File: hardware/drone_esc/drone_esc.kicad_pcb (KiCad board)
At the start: 2 copper layers, 166 parts, among them Q1 BSC016N04LS, Q10 BSC016N04LS, Q11 BSC016N04LS, Q12 BSC016N04LS, Q13 BSC016N04LS, Q14 BSC016N04LS, Q15 BSC016N04LS, Q16 BSC016N04LS, Q17 BSC016N04LS, Q18 BSC016N04LS, Q19 BSC016N04LS, Q2 BSC016N04LS, Q20 BSC016N04LS, Q21 BSC016N04LS, Q22 BSC016N04LS, Q23 BSC016N04LS, Q24 BSC016N04LS, Q3 BSC016N04LS, Q4 BSC016N04LS, Q5 BSC016N04LS, Q6 BSC016N04LS, Q7 BSC016N04LS, Q8 BSC016N04LS, Q9 BSC016N04LS, U1 AMS1117-3.3, U10 FD6288Q, U2 INA180A3, U3 STM32G071GBUxN, U4 FD6288Q, U5 STM32G071GBU6, U6 FD6288Q, U7 FD6288Q, U8 STM32G071GBU6, U9 STM32G071GBU6

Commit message: continued developing the pcb board
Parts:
- C12, C14, C16, C21, C22, C23, C31, C32, C33, C47, C48, C49: value 47uF 35V X7R MLCC -> 22uF 25V X5R MLCC; footprint Capacitor_SMD:C_2220_5750Metric -> Capacitor_SMD:C_1210_3225Metric; moved to B.Cu
- moved C12 92.1 mm to (-8.50, -9.00), turned to 90 degrees
- moved C14 90.4 mm to (-8.50, 9.00), turned to 90 degrees
- moved C33 86.7 mm to (-4.00, -13.0), turned to 180 degrees
- moved C16 78.3 mm to (4.00, 13.0), turned to 180 degrees
- moved C31 73.0 mm to (8.50, -9.00), turned to 90 degrees
- moved C32 72.9 mm to (8.50, -3.00), turned to 90 degrees
- moved C48 53.8 mm to (-8.50, 3.00), turned to 90 degrees
- moved C47 53.4 mm to (-8.50, -3.00), turned to 90 degrees
- moved C49 48.4 mm to (-4.00, 13.0), turned to 180 degrees
- moved C21 35.2 mm to (4.00, -13.0), turned to 180 degrees
- moved C22 32.5 mm to (8.50, 3.00), turned to 90 degrees
- moved C23 32.3 mm to (8.50, 9.00), turned to 90 degrees

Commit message: continued developing the pcb board
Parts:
- C1, C2: value 22uF 25V X7R MLCC -> 22uF 25V X5R MLCC; moved to B.Cu
- Q11, Q9, U1, U2: moved to B.Cu
- moved U2 107.1 mm to (0.00, -17.0), turned to 90 degrees
- moved U1 89.4 mm to (-0.07, 19.5), turned to 90 degrees
- moved Q11 87.0 mm to (-18.7, 3.00), turned to 90 degrees
- moved C2 84.0 mm to (-0.07, 13.0), turned to 180 degrees
- moved C1 80.5 mm to (-0.07, 26.0)
- moved Q9 76.4 mm to (-18.7, 9.00), turned to 90 degrees
- moved Q7 74.1 mm to (-19.3, 26.4), turned to 90 degrees
- moved U10 9.57 mm to (53.5, 25.0)
- moved C16 1.50 mm to (5.50, 13.0)
- moved C49 1.50 mm to (-5.50, 13.0), turned to 0 degrees

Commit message: finnished component placement
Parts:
- added TP11: V, Drone_components:Rectangle test point, F.Cu at (-4.10, -23.1)
- C10, C27, C29, C30, C37, C39, C40, C53, C55, C56, C8, C9: value 0.47uF 25V X7R MLCC -> 1uF 25V X5R MLCC; footprint Capacitor_SMD:C_0603_1608Metric -> Capacitor_SMD:C_0402_1005Metric
- C11, C28, C38, C54: value 4.7uF 25V X7R MLCC -> 10uF 25V X5R MLCC; footprint Capacitor_SMD:C_1206_3216Metric -> Capacitor_SMD:C_0603_1608Metric
- C18, C41, C44, C5: value 4.7uF 10V X7R MLCC -> 4.7uF 10V X5R MLCC; footprint Capacitor_SMD:C_0603_1608Metric -> Capacitor_SMD:C_0402_1005Metric
- C19, C42, C45, C7: footprint Capacitor_SMD:C_01005_0402Metric -> Capacitor_SMD:C_0402_1005Metric
- C3, C4, Q1, Q13, Q15, Q17, Q19, Q21, Q23, Q3, Q5, Q7, R1: moved to B.Cu
- D1, D10, D11, D12, D2, D3, D4, D5, D6, D7, D8, D9: value BAT165 -> RB520S30; footprint Drone_components:BAT165 -> Drone_components:RB520S30
- R15: value YLR25-4-0.25F-W -> ~
- moved TP1 129.2 mm to (-9.11, -4.57)
- moved C7 125.5 mm to (-3.80, -1.18), turned to 90 degrees
- moved C6 125.4 mm to (-5.40, -1.68)
- moved U3 121.5 mm to (-5.14, -4.88), turned to 90 degrees
- moved C5 120.7 mm to (-5.40, -0.65)
- moved C10 118.5 mm to (-11.5, -12.8)
- moved Q3 117.4 mm to (-20.1, -9.00), turned to 90 degrees
- moved C9 117.1 mm to (-11.5, -10.4)
- moved C8 116.0 mm to (-11.5, -8.01)
- moved Q5 113.9 mm to (-8.10, -17.5), turned to 90 degrees
- moved D3 113.8 mm to (-11.2, -11.6), turned to 180 degrees
- moved C42 112.9 mm to (3.78, -14.3), turned to -90 degrees
- moved D2 112.3 mm to (-11.2, -9.21), turned to 180 degrees
- moved R1 111.7 mm to (-2.08, -20.6), turned to 90 degrees
- moved C45 111.4 mm to (3.73, 1.16), turned to -90 degrees
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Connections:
- R15 pad 1: Net-(U2-+) -> VCC
- U2 pad 3: Net-(U2-+) -> VCC
- U2 pad 4: Net-(U2--) -> GND
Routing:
- net GND: track 0.00 -> 10.8 mm, vias 0 -> 2
- net Net-(U4-VB1): track 0.00 -> 7.80 mm
- net LIN1C: track 0.00 -> 6.05 mm
- net Net-(U4-VB2): track 0.00 -> 5.99 mm
- net Net-(U4-VB3): track 0.00 -> 5.56 mm
- net /MCU1/SWDIO: track 0.00 -> 5.18 mm
- net /ESC1/VS3: track 0.00 -> 5.14 mm
- net +3.3V: track 0.00 -> 4.52 mm, vias 0 -> 2
- net /ESC1/VS1: track 0.00 -> 4.51 mm
- net LIN1B: track 0.00 -> 4.42 mm
- net /ESC1/VS2: track 0.00 -> 4.31 mm
- net /MCU1/SWCLK: track 0.00 -> 2.98 mm
- net VCC: track 0.00 -> 2.96 mm, vias 0 -> 1
- net LIN1A: track 0.00 -> 2.89 mm
- net /ESC1/LO2: track 0.00 -> 2.57 mm
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
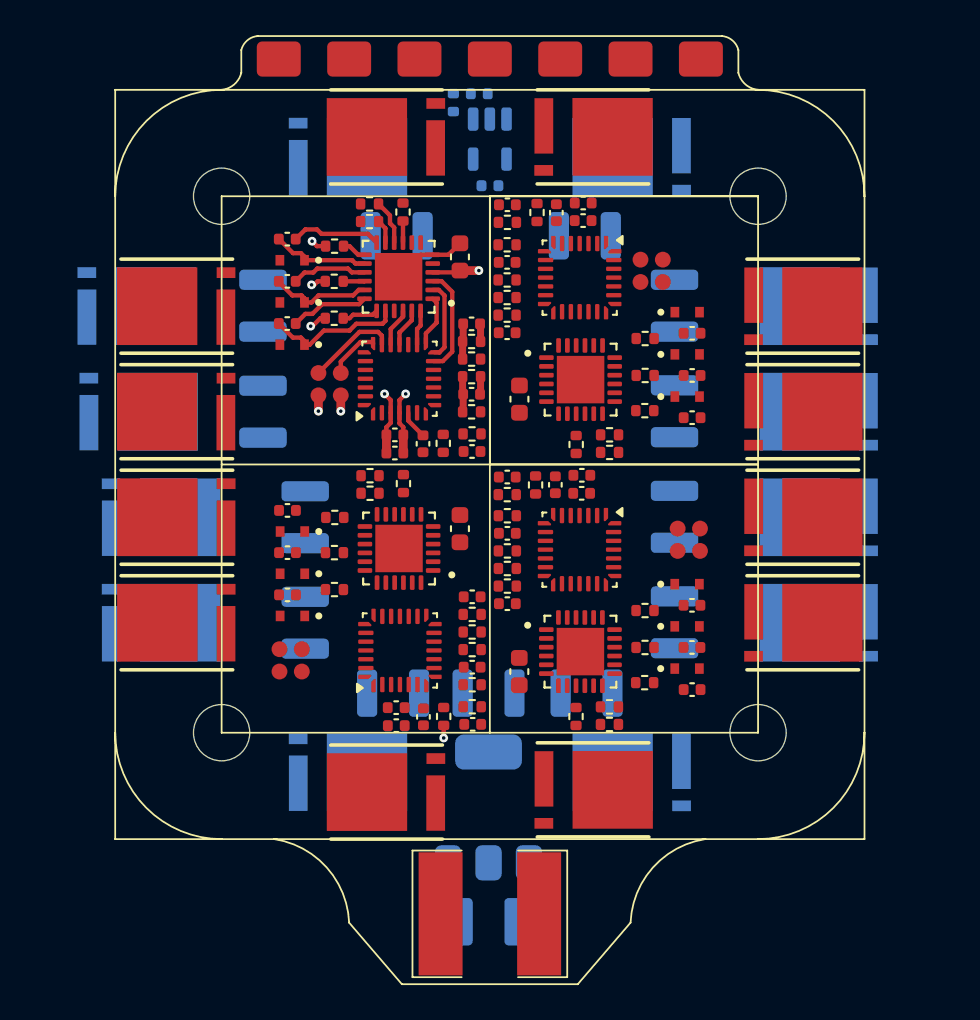
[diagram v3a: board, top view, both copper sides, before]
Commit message: need to connect the shunt resistor/ via stiching/ and finish power layer
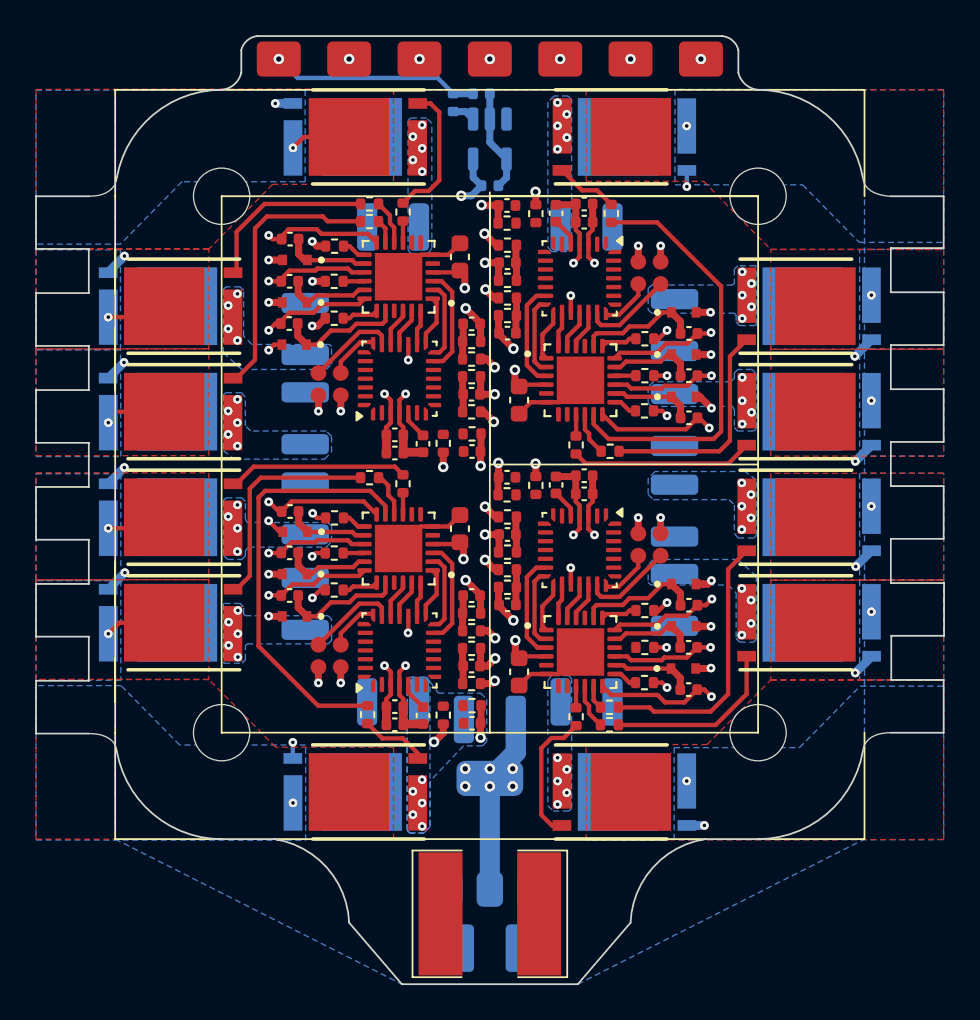
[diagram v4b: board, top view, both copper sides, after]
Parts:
- moved R28 12.6 mm to (6.90, -14.3), turned to 90 degrees
- moved R16 12.6 mm to (-6.95, 14.2), turned to -90 degrees
- moved C12 2.74 mm to (-10.5, -7.70)
- moved C47 2.43 mm to (-10.5, -2.62)
- moved TP10 2.25 mm to (9.07, 4.55), turned to 180 degrees
- moved TP6 2.23 mm to (-9.11, 10.9)
- moved C1 1.50 mm to (0.00, 27.5)
- moved C2 1.50 mm to (0.00, 14.5)
- moved U1 1.50 mm to (0.00, 21.0)
- moved C23 1.27 mm to (10.5, 7.70), turned to 90 degrees
- moved Q3 1.22 mm to (-18.9, -9.00)
- moved Q13 1.16 mm to (8.40, -18.6)
- moved Q23 1.16 mm to (8.40, 18.6)
- moved Q5 1.16 mm to (-8.40, -18.6)
- moved Q7 1.16 mm to (-8.40, 18.6)
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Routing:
- net GND: track 10.8 -> 70.1 mm, vias 2 -> 77
- net /ESC2/VS3: track 0.00 -> 39.4 mm, vias 0 -> 3
- net /ESC2/VS2: track 0.00 -> 38.6 mm, vias 0 -> 3
- net /ESC3/VS2: track 0.00 -> 36.3 mm, vias 0 -> 3
- net /ESC1/VS2: track 4.31 -> 39.1 mm, vias 0 -> 3
- net /ESC4/VS1: track 0.00 -> 34.5 mm, vias 0 -> 3
- net /ESC3/VS3: track 0.00 -> 34.0 mm, vias 0 -> 3
- net /ESC4/VS2: track 0.00 -> 33.0 mm, vias 0 -> 3
- net /ESC1/VS1: track 4.51 -> 37.2 mm, vias 0 -> 3
- net /ESC3/VS1: track 0.00 -> 30.1 mm, vias 0 -> 3
- net /ESC4/VS3: track 0.00 -> 29.8 mm, vias 0 -> 3
- net /ESC1/VS3: track 5.14 -> 34.5 mm, vias 0 -> 3
- net /ESC2/VS1: track 0.71 -> 29.8 mm, vias 1 -> 3
- net +3.3V: track 4.52 -> 31.4 mm, vias 2 -> 16
- net /ESC3/LO1: track 0.00 -> 24.3 mm
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- added copper zone on B.Cu, net /ESC1/VS1
- added copper zone on F.Cu, net /ESC1/VS1
- added copper zone on B.Cu, net /ESC1/VS2
- added copper zone on F.Cu, net /ESC1/VS2
- added copper zone on B.Cu, net /ESC1/VS3
- added copper zone on F.Cu, net /ESC1/VS3
- added copper zone on B.Cu, net /ESC2/VS1
- added copper zone on F.Cu, net /ESC2/VS1
- added copper zone on B.Cu, net /ESC2/VS2
- added copper zone on F.Cu, net /ESC2/VS2
- added copper zone on B.Cu, net /ESC2/VS3
- added copper zone on F.Cu, net /ESC2/VS3
- added copper zone on B.Cu, net /ESC3/VS1
- added copper zone on F.Cu, net /ESC3/VS1
- added copper zone on B.Cu, net /ESC3/VS2
- added copper zone on F.Cu, net /ESC3/VS2
- added copper zone on B.Cu, net /ESC3/VS3
- added copper zone on F.Cu, net /ESC3/VS3
- added copper zone on B.Cu, net /ESC4/VS1
- added copper zone on F.Cu, net /ESC4/VS1
- added copper zone on B.Cu, net /ESC4/VS2
- added copper zone on F.Cu, net /ESC4/VS2
- added copper zone on B.Cu, net /ESC4/VS3
- added copper zone on F.Cu, net /ESC4/VS3
- added copper zone on B.Cu, net GND
- added copper zone on In1.Cu, net GND
- added copper zone on In4.Cu, net GND
- added copper zone on B.Cu, net VCC
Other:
- board outline added: 51.6 x 53.9 mm
- copper layers 2 -> 6

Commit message: replaced some of the schematics
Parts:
- C1, C12, C14, C16, C2, C21, C22, C23, C31, C32, C33, C47, C48, C49: footprint Capacitor_SMD:C_1210_3225Metric -> Capacitor_SMD:C_0805_2012Metric; moved to F.Cu
- C3, C4, R1, U1, U2: moved to F.Cu
- Q1, Q11, Q13, Q15, Q17, Q19, Q21, Q23, Q3, Q5, Q7, Q9: value BSC016N04LS -> BSC009NE2LS5IATMA1; footprint Drone_components:BSC016N04LS -> Drone_components:BSC093N04LSGATMA1; moved to F.Cu
- Q10, Q12, Q14, Q16, Q18, Q2, Q20, Q22, Q24, Q4, Q6, Q8: value BSC016N04LS -> BSC009NE2LS5IATMA1; footprint Drone_components:BSC016N04LS -> Drone_components:BSC093N04LSGATMA1
- R10, R11, R2, R3, R6, R7: value 33 -> 10
- R14, R16, R17, R18, R19, R20, R27, R28, R29, R30, R31, R32, R39, R40, R41, R42, R43, R44: value 33 -> 47
- moved Q6 142.7 mm to (134.2, 2.75), turned to 0 degrees
- moved Q4 138.7 mm to (120.8, 2.75), turned to 0 degrees
- moved Q5 137.6 mm to (127.5, 2.75), turned to 0 degrees
- moved Q3 133.5 mm to (114.1, 2.75), turned to 0 degrees
- moved TP4 131.8 mm to (99.1, 47.8)
- moved TP9 130.7 mm to (119.6, 51.1)
- moved U2 130.2 mm to (113.3, 45.7), turned to 0 degrees
- moved C45 129.9 mm to (125.6, 46.3), turned to 0 degrees
- moved D3 129.0 mm to (115.6, 13.0), turned to 0 degrees
- moved C46 128.9 mm to (125.6, 48.3), turned to 0 degrees
- moved D2 128.2 mm to (115.6, 10.7), turned to 0 degrees
- moved U4 127.9 mm to (121.0, 10.3), turned to 0 degrees
- moved C44 127.9 mm to (125.6, 44.3), turned to 0 degrees
- moved D1 127.6 mm to (115.6, 8.31), turned to 0 degrees
- moved Q24 127.5 mm to (134.2, 25.1), turned to 0 degrees
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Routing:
- net GND: track 70.1 -> 0.00 mm, vias 77 -> 0
- net /ESC1/VS2: track 39.1 -> 0.00 mm, vias 3 -> 0
- net +3.3V: track 31.4 -> 0.00 mm, vias 16 -> 0
- net /ESC1/VS1: track 37.2 -> 68.5 mm, vias 3 -> 0
- net /ESC3/LO1: track 24.3 -> 0.00 mm
- net /ESC2/LO1: track 24.3 -> 0.00 mm
- net VCC: track 20.9 -> 0.00 mm, vias 16 -> 3
- net Net-(Q2-Pad4): track 15.4 -> 0.00 mm
- net Net-(Q20-Pad4): track 15.3 -> 0.00 mm
- net Net-(Q1-Pad4): track 14.2 -> 0.00 mm, vias 2 -> 0
- net Net-(Q16-Pad4): track 12.7 -> 0.00 mm
- net Net-(Q10-Pad4): track 12.6 -> 0.00 mm
- net Net-(C4-Pad1): track 11.9 -> 0.00 mm, vias 1 -> 0
- net /ESC2/VS3: track 39.4 -> 27.9 mm, vias 3 -> 0
- net /ESC1/VS3: track 34.5 -> 23.3 mm, vias 3 -> 0
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- removed copper zone on B.Cu, net /ESC1/VS1
- removed copper zone on F.Cu, net /ESC1/VS1
- removed copper zone on B.Cu, net /ESC1/VS2
- removed copper zone on F.Cu, net /ESC1/VS2
- removed copper zone on B.Cu, net /ESC1/VS3
- removed copper zone on F.Cu, net /ESC1/VS3
- removed copper zone on B.Cu, net /ESC2/VS1
- removed copper zone on F.Cu, net /ESC2/VS1
- removed copper zone on B.Cu, net /ESC2/VS2
- removed copper zone on F.Cu, net /ESC2/VS2
- removed copper zone on B.Cu, net /ESC2/VS3
- removed copper zone on F.Cu, net /ESC2/VS3
- removed copper zone on B.Cu, net /ESC3/VS1
- removed copper zone on F.Cu, net /ESC3/VS1
- removed copper zone on B.Cu, net /ESC3/VS2
- removed copper zone on F.Cu, net /ESC3/VS2
- removed copper zone on B.Cu, net /ESC3/VS3
- removed copper zone on F.Cu, net /ESC3/VS3
- removed copper zone on B.Cu, net /ESC4/VS1
- removed copper zone on F.Cu, net /ESC4/VS1
- removed copper zone on B.Cu, net /ESC4/VS2
- removed copper zone on F.Cu, net /ESC4/VS2
- removed copper zone on B.Cu, net /ESC4/VS3
- removed copper zone on F.Cu, net /ESC4/VS3
- removed copper zone on B.Cu, net GND
- removed copper zone on B.Cu, net VCC

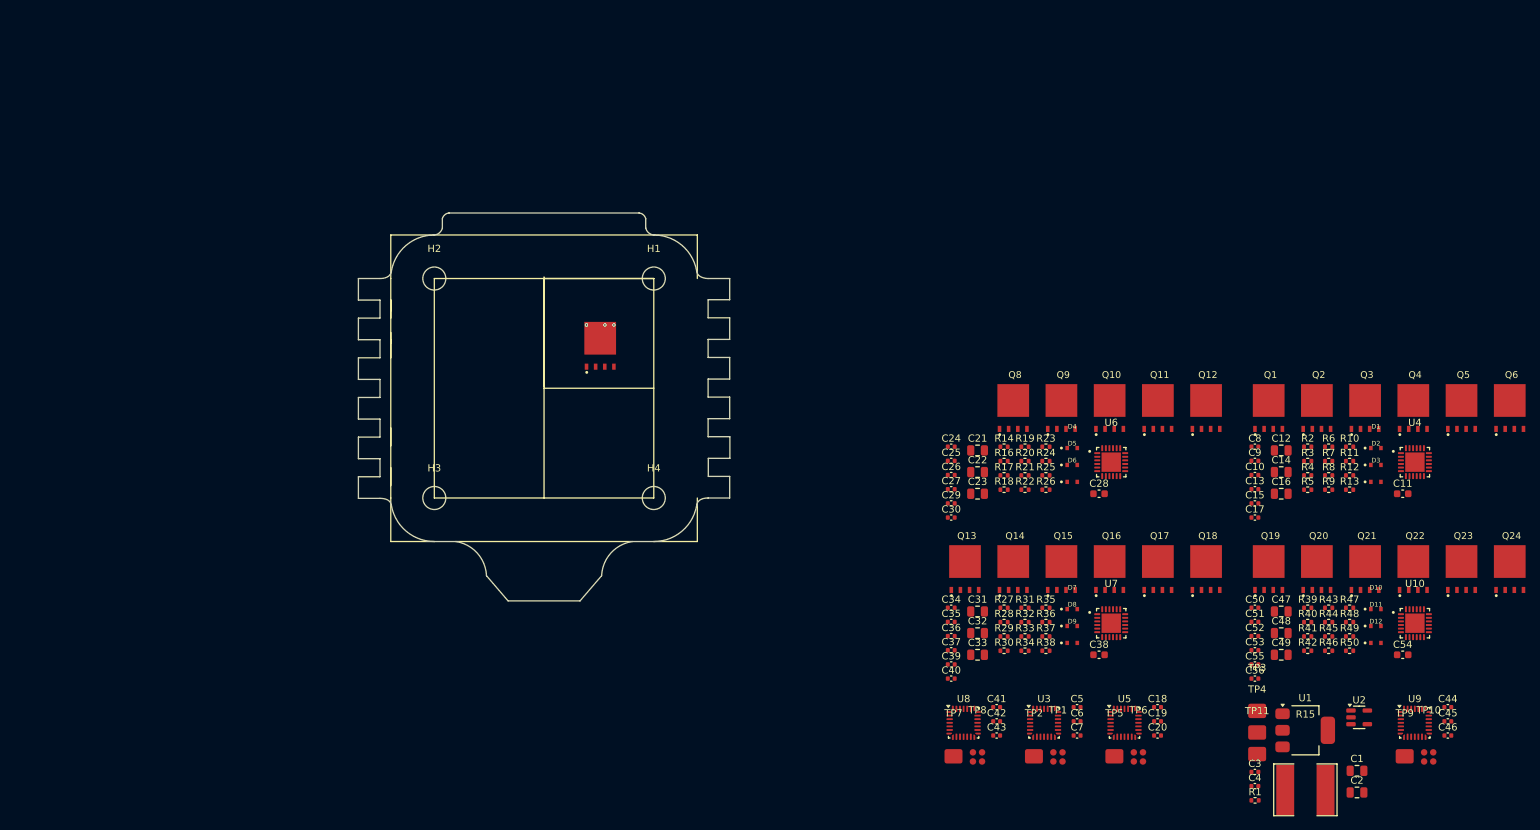
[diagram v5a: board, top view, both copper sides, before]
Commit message: changed some footprints and reconstracted the latout with better gate resistors clearence
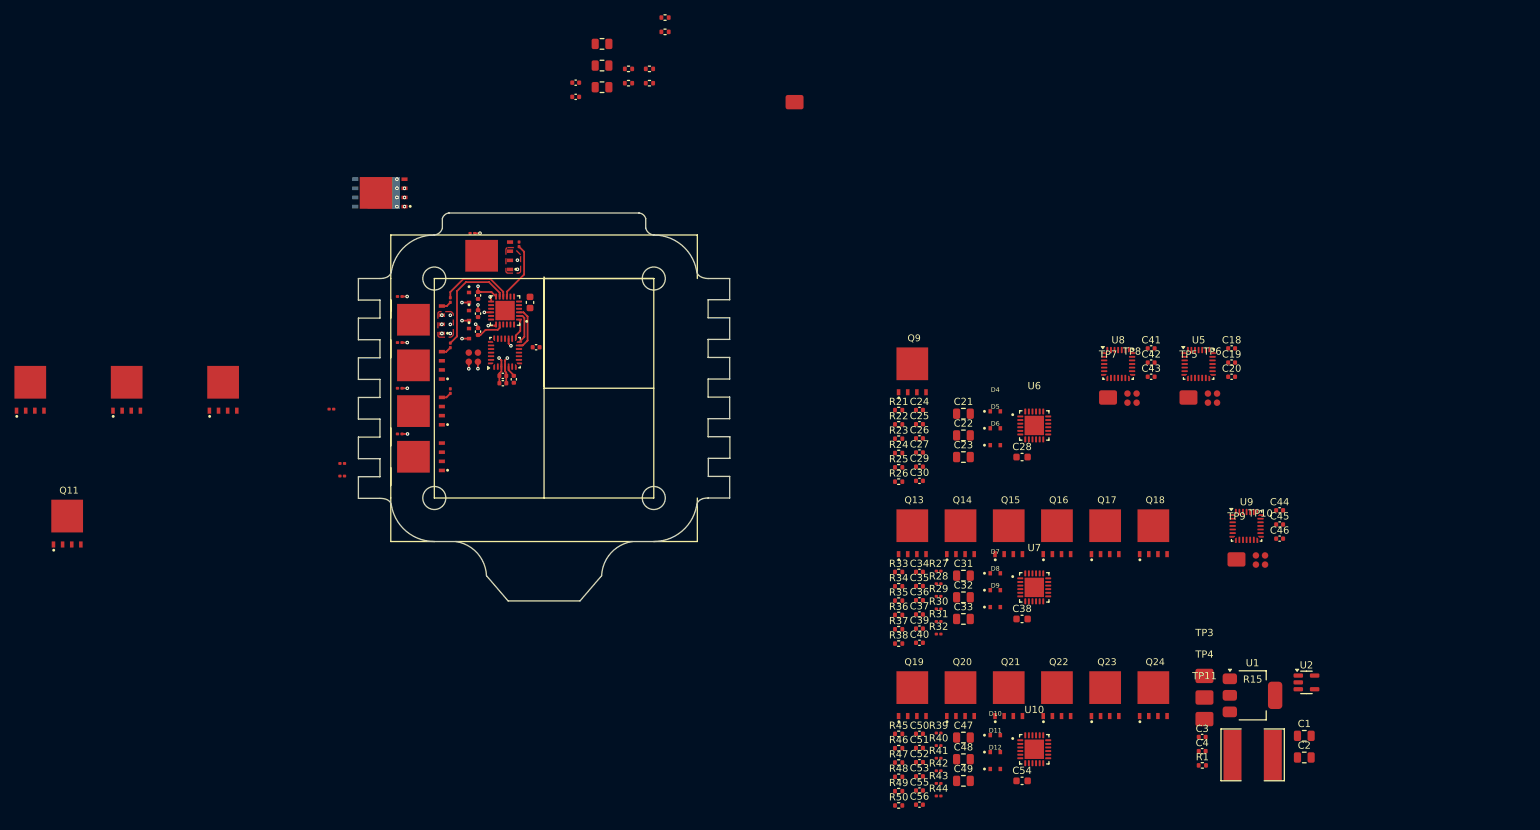
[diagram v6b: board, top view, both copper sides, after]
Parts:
- Q7: moved to B.Cu
- R10, R11, R2, R3, R6, R7: footprint Resistor_SMD:R_0402_1005Metric -> Resistor_SMD:R_0201_0603Metric
- R14, R16, R17, R18, R19, R20, R27, R28, R29, R30, R31, R32, R39, R40, R41, R42, R43, R44: value 47 -> 10; footprint Resistor_SMD:R_0402_1005Metric -> Resistor_SMD:R_0201_0603Metric
- moved Q1 172.1 mm to (-71.4, 0.22)
- moved Q3 172.1 mm to (-58.0, 0.22)
- moved Q5 172.1 mm to (-44.6, 0.22)
- moved Q11 152.4 mm to (-66.3, 18.8)
- moved Q6 143.4 mm to (-7.62, -18.4), turned to 90 degrees
- moved Q4 138.4 mm to (-17.1, -9.52), turned to 90 degrees
- moved R6 130.8 mm to (-20.1, -12.8), turned to 180 degrees
- moved D3 128.6 mm to (-10.4, -12.6), turned to -90 degrees
- moved U4 128.2 mm to (-5.42, -10.8), turned to 180 degrees
- moved D2 127.7 mm to (-10.4, -10.1), turned to -90 degrees
- moved D1 127.0 mm to (-10.4, -7.60), turned to -90 degrees
- moved R2 127.0 mm to (-20.1, -6.35), turned to 180 degrees
- moved R10 125.5 mm to (-9.96, -21.5), turned to 180 degrees
- moved Q2 124.6 mm to (-17.1, -3.18), turned to 90 degrees
- moved C11 124.2 mm to (-1.95, -11.9), turned to -90 degrees
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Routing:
- net /ESC1/VS1: track 68.5 -> 9.96 mm, vias 0 -> 1
- net /ESC3/VS2: track 29.3 -> 0.00 mm
- net /ESC2/VS2: track 28.4 -> 0.00 mm
- net /ESC2/VS3: track 27.9 -> 0.00 mm
- net /ESC4/VS1: track 27.6 -> 0.00 mm
- net /ESC3/VS3: track 26.1 -> 0.00 mm
- net /ESC4/VS2: track 26.1 -> 0.00 mm
- net /ESC3/VS1: track 23.3 -> 0.00 mm
- net /ESC2/VS1: track 23.0 -> 0.00 mm
- net /ESC4/VS3: track 21.4 -> 0.00 mm
- net /ESC1/LO1: track 0.00 -> 15.2 mm
- net /ESC1/HO1: track 0.00 -> 14.8 mm, vias 0 -> 2
- net /ESC1/VS2: track 0.00 -> 14.0 mm, vias 0 -> 1
- net /ESC1/HO2: track 0.00 -> 14.0 mm, vias 0 -> 2
- net Net-(Q19-Pad4): track 12.0 -> 0.00 mm
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- added copper zone on F.Cu, net GND
- removed copper zone on In1.Cu, net GND
- removed copper zone on In4.Cu, net GND
